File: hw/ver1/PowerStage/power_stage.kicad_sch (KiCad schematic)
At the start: 93 parts, among them J7 Conn_01x02_Socket, Q3 BSS138, Q4 BSS138, Q5 BSS84, Q6 BSS138, U11 74AHC1G126, U12 74AHC1G126, U13 74AHC1G126, U14 74AHC1G126, U15 74AHC1G126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

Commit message: Sync lunch work
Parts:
- U3: footprint Package_QFP:LQFP-64-1EP_10x10mm_P0.5mm_EP6.5x6.5mm -> Package_QFP:LQFP-64-1EP_10x10mm_P0.5mm_EP6.5x6.5mm_ThermalVias
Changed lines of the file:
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@@
 			)
 		)
-		(property "Footprint" "Package_QFP:LQFP-64-1EP_10x10mm_P0.5mm_EP6.5x6.5mm"
+		(property "Footprint" "Package_QFP:LQFP-64-1EP_10x10mm_P0.5mm_EP6.5x6.5mm_ThermalVias"
 			(at 156.21 139.446 0)
 			(effects

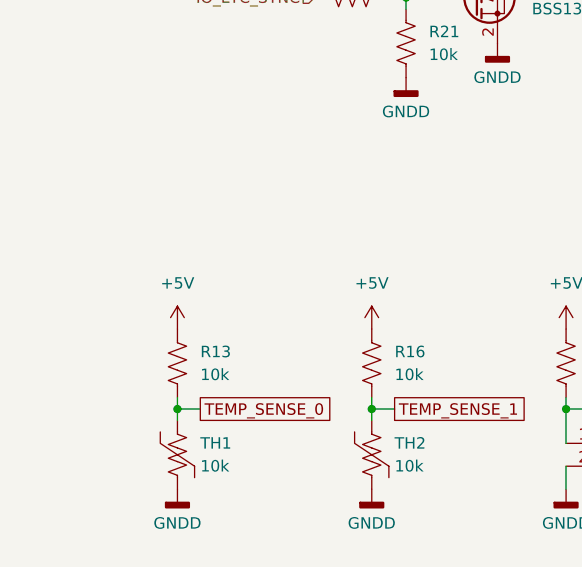
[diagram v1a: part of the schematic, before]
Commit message: Improve low voltage power layout
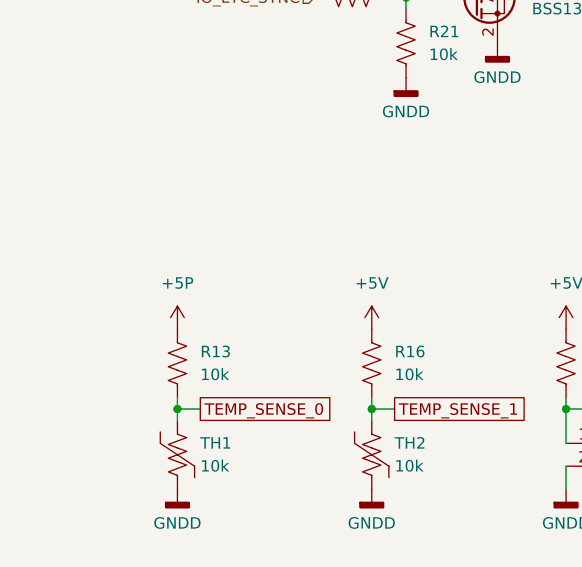
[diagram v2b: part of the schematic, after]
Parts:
- U3: footprint Package_QFP:LQFP-64-1EP_10x10mm_P0.5mm_EP6.5x6.5mm_ThermalVias -> Package_QFP:LQFP-64-1EP_10x10mm_P0.5mm_EP6.5x6.5mm
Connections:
- net +5P: now also R13.2
- net +5V: no longer R13.2
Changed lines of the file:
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@@
+	)
+	(symbol
+		(lib_id "power:+5P")
+		(at 52.07 228.6 0)
+		(unit 1)
+		(exclude_from_sim no)
+		(in_bom yes)
+		(on_board yes)
+		(dnp no)
+		(property "Reference" "#PWR03"
+			(at 52.07 232.41 0)
+			(effects
+				(font
+					(size 1.27 1.27)
+				)
+				(hide yes)
+			)
+		)
+		(property "Value" "+5P"
+			(at 52.07 223.52 0)
+			(effects
+				(font
+					(size 1.27 1.27)
+				)
+			)
+		)
+		(property "Footprint" ""
+			(at 52.07 228.6 0)
+			(effects
+				(font
+					(size 1.27 1.27)
+				)
+				(hide yes)
+			)
+		)
+		(property "Datasheet" ""
+			(at 52.07 228.6 0)
+			(effects
+				(font
+					(size 1.27 1.27)
+				)
+				(hide yes)
+			)
+		)
+		(property "Description" "Power symbol creates a global label with name \"+5P\""
+			(at 52.07 228.6 0)
+			(effects
+				(font
+					(size 1.27 1.27)
+				)
+				(hide yes)
+			)
+		)
+		(pin "1"
+		)
+		(instances
+			(project "IchnaeaV1"
+				(path "/1a8ad36a-4b76-4949-97c2-661f12a0b1d9/2acacade-9567-40f5-9827-bf22bd24fca6"
+					(reference "#PWR03")
+					(unit 1)
+				)
+			)
+		)
 	)
 	(symbol
@@
 			)
 		)
-		(property "Footprint" "Package_QFP:LQFP-64-1EP_10x10mm_P0.5mm_EP6.5x6.5mm_ThermalVias"
+		(property "Footprint" "Package_QFP:LQFP-64-1EP_10x10mm_P0.5mm_EP6.5x6.5mm"
 			(at 156.21 139.446 0)
 			(effects
@@
 					(unit 1)
 				)
-			)
-		)
-	)
-	(symbol
-		(lib_id "power:+5V")
-		(at 52.07 228.6 0)
-		(unit 1)
-		(exclude_from_sim no)
-		(in_bom yes)
-		(on_board yes)
-		(dnp no)
-		(fields_autoplaced yes)
-		(property "Reference" "#PWR03"
-			(at 52.07 232.41 0)
-			(effects
-				(font
-					(size 1.27 1.27)
-				)
-				(hide yes)
-			)
-		)
-		(property "Value" "+5V"
-			(at 52.07 223.52 0)
-			(effects
-				(font
-					(size 1.27 1.27)
-				)
-			)
-		)
-		(property "Footprint" ""
-			(at 52.07 228.6 0)
-			(effects
-				(font
-					(size 1.27 1.27)
-				)
-				(hide yes)
-			)
-		)
-		(property "Datasheet" ""
-			(at 52.07 228.6 0)
-			(effects
-				(font
-					(size 1.27 1.27)
-				)
-				(hide yes)
-			)
-		)
-		(property "Description" "Power symbol creates a global label with name \"+5V\""
-			(at 52.07 228.6 0)
-			(effects
-				(font
-					(size 1.27 1.27)
-				)
-				(hide yes)
-			)
-		)
-		(pin "1"
-		)
-		(instances
-			(project "IchnaeaV1"
-				(path "/1a8ad36a-4b76-4949-97c2-661f12a0b1d9/2acacade-9567-40f5-9827-bf22bd24fca6"
-					(reference "#PWR03")
-					(unit 1)
-				)

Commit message: Sync work
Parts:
- removed J7: Conn_01x02_Socket, Connector_PinSocket_2.54mm:PinSocket_1x02_P2.54mm_Vertical, symbol Connector:Conn_01x02_Socket
- removed R20, R6, R8, R9: 10k, Resistor_SMD:R_0603_1608Metric, symbol Device:R_US
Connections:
- net TEMP_SENSE_2: no longer names the net of U2.12 (A3)
- no-connect marks 4 -> 5

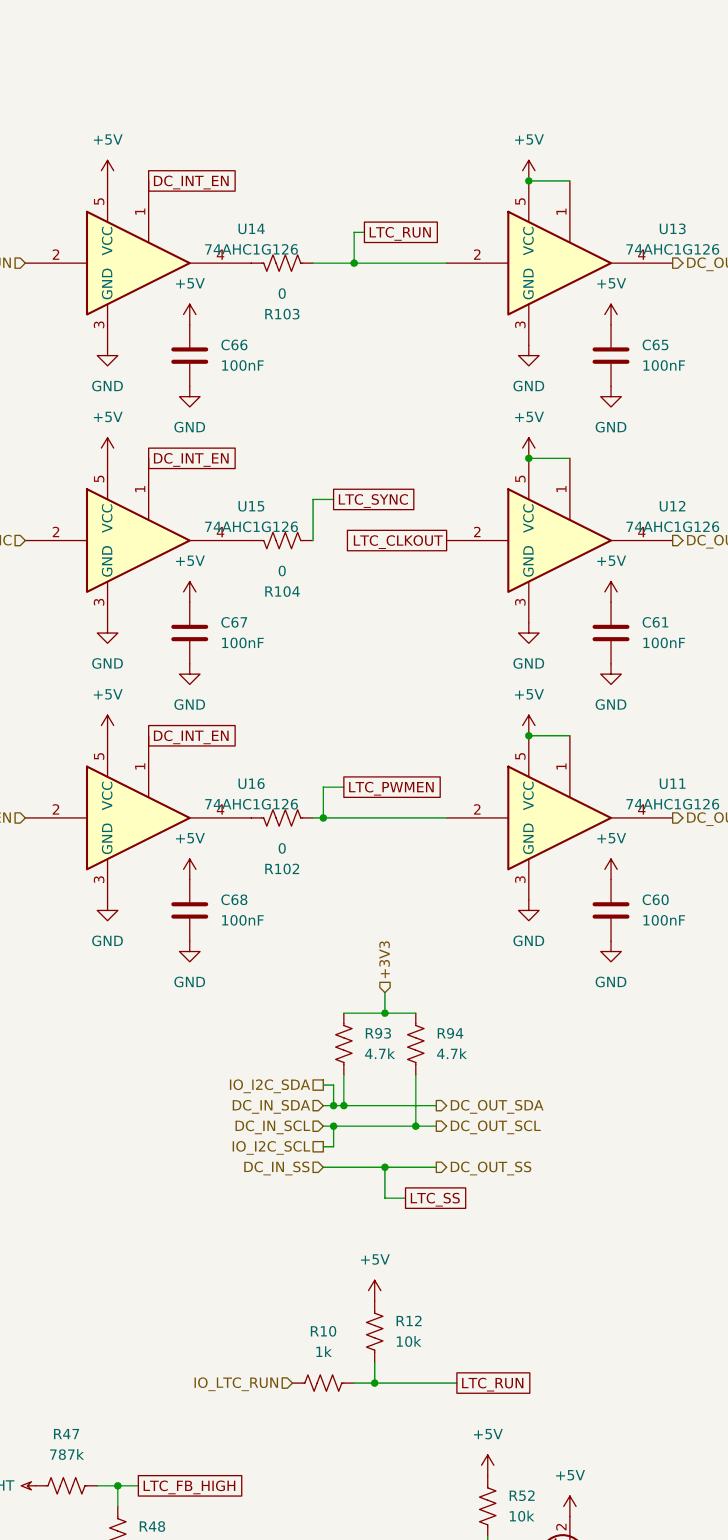
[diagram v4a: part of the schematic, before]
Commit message: Finish the initial route before DRC
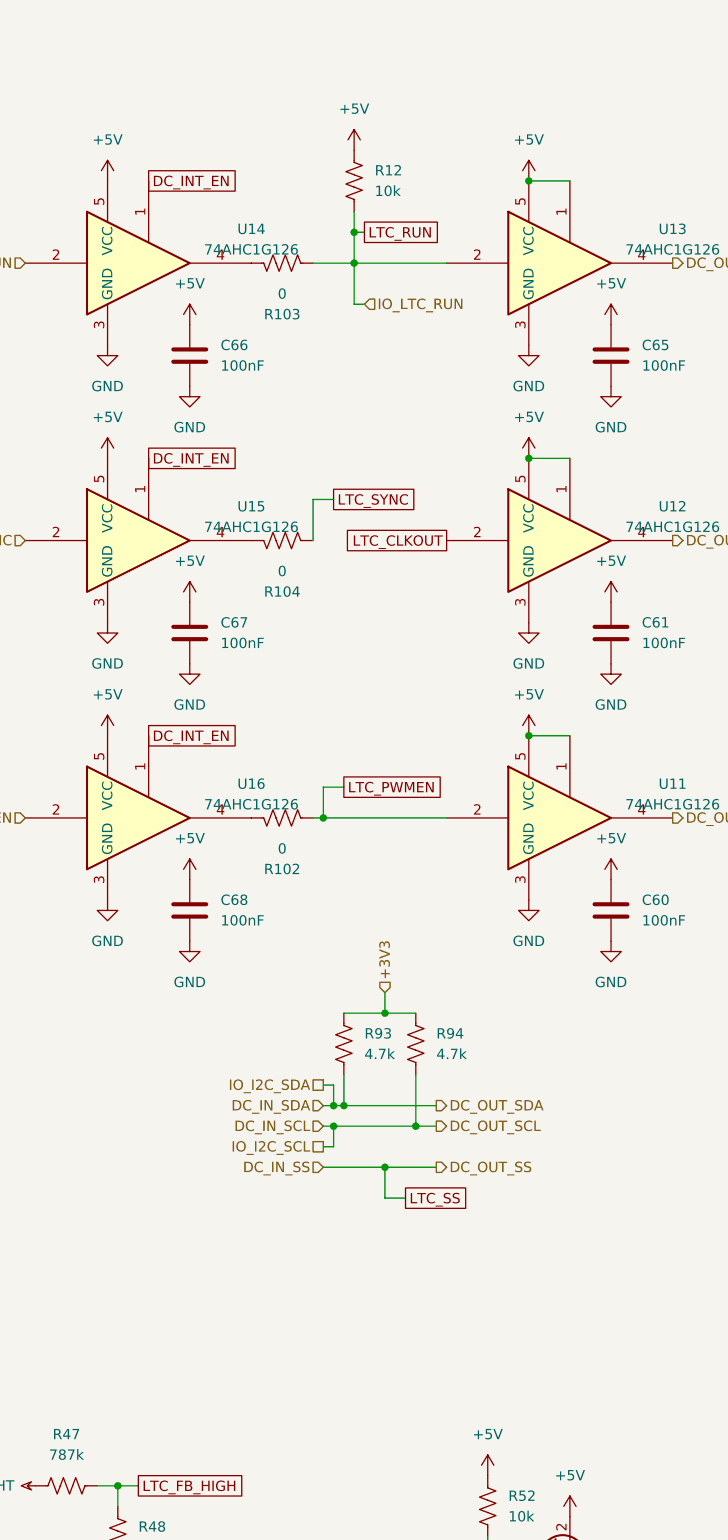
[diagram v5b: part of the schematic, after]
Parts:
- removed R10: 1k, Resistor_SMD:R_0603_1608Metric, symbol Device:R_US
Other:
- moved on the sheet: R12
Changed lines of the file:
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@@
 	)
 	(junction
-		(at 354.33 181.61)
+		(at 373.38 33.02)
 		(diameter 0)
 		(color 0 0 0 0)
 	)
 	(junction
-		(at 373.38 33.02)
+		(at 351.79 39.37)
 		(diameter 0)
 		(color 0 0 0 0)
@@
 	(wire
 		(pts
-			(xy 354.33 179.07) (xy 354.33 181.61)
-		)
-		(stroke
-			(width 0)
-			(type default)
-		)
-	)
-	(wire
-		(pts
 			(xy 215.9 191.77) (xy 215.9 193.04)
 		)
@@
 	(wire
 		(pts
+			(xy 351.79 48.26) (xy 351.79 43.18)
+		)
+		(stroke
+			(width 0)
+			(type default)
+		)
+	)
+	(wire
+		(pts
 			(xy 142.24 233.68) (xy 142.24 229.87)
 		)
@@
 	(wire
 		(pts
-			(xy 354.33 181.61) (xy 364.49 181.61)
-		)
-		(stroke
-			(width 0)
-			(type default)
-		)
-	)
-	(wire
-		(pts
 			(xy 189.23 118.11) (xy 199.39 118.11)
 		)
@@
 	(wire
 		(pts
-			(xy 351.79 181.61) (xy 354.33 181.61)
+			(xy 154.94 133.35) (xy 153.67 133.35)
 		)
 		(stroke
@@
 	(wire
 		(pts
-			(xy 154.94 133.35) (xy 153.67 133.35)
+			(xy 83.82 156.21) (xy 83.82 157.48)
 		)
 		(stroke
@@
 	(wire
 		(pts
-			(xy 83.82 156.21) (xy 83.82 157.48)
+			(xy 351.79 36.83) (xy 351.79 39.37)
 		)
 		(stroke
@@
 	(wire
 		(pts
+			(xy 353.06 48.26) (xy 351.79 48.26)
+		)
+		(stroke
+			(width 0)
+			(type default)
+		)
+	)
+	(wire
+		(pts
 			(xy 260.35 99.06) (xy 260.35 100.33)
 		)
@@
 		)
 	)
-	(global_label "LTC_RUN"
-		(shape passive)
-		(at 364.49 181.61 0)
-		(fields_autoplaced yes)
-		(effects
-			(font
-				(size 1.27 1.27)
-			)
-			(justify left)
-		)
-		(property "Intersheetrefs" "${INTERSHEET_REFS}"
-			(at 374.5282 181.61 0)
-			(effects
-				(font
-					(size 1.27 1.27)
-				)
-				(justify left)
-				(hide yes)
-			)
-		)
-	)
 	(global_label "LTC_ILIM"
 		(shape passive)
@@
 	(hierarchical_label "IO_LTC_RUN"
 		(shape input)
-		(at 344.17 181.61 180)
+		(at 353.06 48.26 0)
 		(fields_autoplaced yes)
 		(effects
@@
 				(size 1.27 1.27)
 			)
-			(justify right)
+			(justify left)
 		)
 	)
@@
 	)
 	(symbol
-		(lib_id "Device:R_US")
-		(at 347.98 181.61 90)
-		(unit 1)
-		(exclude_from_sim no)
-		(in_bom yes)
-		(on_board yes)
-		(dnp no)
-		(fields_autoplaced yes)
-		(property "Reference" "R10"
-			(at 347.98 175.26 90)
-			(effects
-				(font
-					(size 1.27 1.27)
-				)
-			)
-		)
-		(property "Value" "1k"
-			(at 347.98 177.8 90)
-			(effects
-				(font
-					(size 1.27 1.27)
-				)
-			)
-		)
-		(property "Footprint" "Resistor_SMD:R_0603_1608Metric"
-			(at 348.234 180.594 90)
-			(effects
-				(font
-					(size 1.27 1.27)
-				)
-				(hide yes)
-			)
-		)
-		(property "Datasheet" "~"
-			(at 347.98 181.61 0)
-			(effects
-				(font
-					(size 1.27 1.27)
-				)
-				(hide yes)
-			)
-		)
-		(property "Description" "Resistor, US symbol"
-			(at 347.98 181.61 0)
-			(effects
-				(font
-					(size 1.27 1.27)
-				)
-				(hide yes)
-			)
-		)
-		(property "Field-1" ""
-			(at 347.98 181.61 0)
-			(effects
-				(font
-					(size 1.27 1.27)
-				)
-				(hide yes)
-			)
-		)
-		(property "Digikey" "N/A"
-			(at 347.98 181.61 0)
-			(effects
-				(font
-					(size 1.27 1.27)
-				)
-				(hide yes)
-			)
-		)
-		(property "LCSC" "C21190"
-			(at 347.98 181.61 0)
-			(effects
-				(font
-					(size 1.27 1.27)
-				)
-				(hide yes)
-			)
-		)
-		(pin "1"
-		)
-		(pin "2"
-		)
-		(instances
-			(project "IchnaeaV1"
-				(path "/1a8ad36a-4b76-4949-97c2-661f12a0b1d9/2acacade-9567-40f5-9827-bf22bd24fca6"
-					(reference "R10")
-					(unit 1)
-				)
-			)
-		)
-	)
-	(symbol
 		(lib_id "Device:D_Schottky")
 		(at 135.89 20.32 180)
@@
 	(symbol
 		(lib_id "power:+5V")
-		(at 354.33 171.45 0)
+		(at 351.79 29.21 0)
 		(unit 1)
 		(exclude_from_sim no)
@@
 		(fields_autoplaced yes)
 		(property "Reference" "#PWR020"
-			(at 354.33 175.26 0)
+			(at 351.79 33.02 0)
 			(effects
 				(font
@@
 		)
 		(property "Value" "+5V"
-			(at 354.33 166.37 0)
+			(at 351.79 24.13 0)
 			(effects
 				(font
@@
 		)
 		(property "Footprint" ""
-			(at 354.33 171.45 0)
+			(at 351.79 29.21 0)
 			(effects
 				(font
@@
 		)
 		(property "Datasheet" ""
-			(at 354.33 171.45 0)
+			(at 351.79 29.21 0)
 			(effects
 				(font
@@
 		)
 		(property "Description" "Power symbol creates a global label with name \"+5V\""
-			(at 354.33 171.45 0)
+			(at 351.79 29.21 0)
 			(effects
 				(font
@@
 	(symbol
 		(lib_id "Device:R_US")
-		(at 354.33 175.26 180)
+		(at 351.79 33.02 180)
 		(unit 1)
 		(exclude_from_sim no)
@@
 		(fields_autoplaced yes)
 		(property "Reference" "R12"
-			(at 356.87 173.9899 0)
+			(at 354.33 31.7499 0)
 			(effects
 				(font
@@
 		)
 		(property "Value" "10k"
-			(at 356.87 176.5299 0)
+			(at 354.33 34.2899 0)
 			(effects
 				(font
@@
 		)
 		(property "Footprint" "Resistor_SMD:R_0603_1608Metric"
-			(at 353.314 175.006 90)
+			(at 350.774 32.766 90)
 			(effects
 				(font
@@
 		)
 		(property "Datasheet" "~"
-			(at 354.33 175.26 0)
+			(at 351.79 33.02 0)
 			(effects
 				(font
@@
 		)
 		(property "Description" "Resistor, US symbol"
-			(at 354.33 175.26 0)
+			(at 351.79 33.02 0)
 			(effects
 				(font
@@
 		)
 		(property "Field-1" ""
-			(at 354.33 175.26 0)
+			(at 351.79 33.02 0)
 			(effects
 				(font
@@
 		)
 		(property "LCSC" "C25804"
-			(at 354.33 175.26 0)
+			(at 351.79 33.02 0)
 			(effects
 				(font
@@
 		)
 		(property "Digikey" "N/A"
-			(at 354.33 175.26 0)
+			(at 351.79 33.02 0)
 			(effects
 				(font

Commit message: Sync lunch work
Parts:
- C19, C20, C23, C24, C58, C59: value 10uF -> 10uF-100V; LCSC (none) -> N/A
- C64: value 10uF -> 10uF-75V; LCSC (none) -> N/A
- TH1, TH2: value 10k -> 10k-NTC
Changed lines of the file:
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@@
 			)
 		)
-		(property "Value" "10uF"
+		(property "Value" "10uF-100V"
 			(at 245.11 27.9399 0)
 			(effects
@@
 			)
 		)
+		(property "LCSC" "N/A"
+			(at 241.3 26.67 0)
+			(effects
+				(font
+					(size 1.27 1.27)
+				)
+				(hide yes)
+			)
+		)
 		(pin "1"
 		)
@@
 			)
 		)
-		(property "Value" "10uF"
+		(property "Value" "10uF-100V"
 			(at 265.43 27.9399 0)
 			(effects
@@
 			)
 		)
+		(property "LCSC" "N/A"
+			(at 261.62 26.67 0)
+			(effects
+				(font
+					(size 1.27 1.27)
+				)
+				(hide yes)
+			)
+		)
 		(pin "1"
 		)
@@
 			)
 		)
-		(property "Value" "10uF"
+		(property "Value" "10uF-100V"
 			(at 224.79 27.9399 0)
 			(effects
@@
 			)
 		)
+		(property "LCSC" "N/A"
+			(at 220.98 26.67 0)
+			(effects
+				(font
+					(size 1.27 1.27)
+				)
+				(hide yes)
+			)
+		)
 		(pin "1"
 		)
@@
 			)
 		)
-		(property "Value" "10uF"
+		(property "Value" "10uF-100V"
 			(at 234.95 27.9399 0)
 			(effects
@@
 			)
 		)
+		(property "LCSC" "N/A"
+			(at 231.14 26.67 0)
+			(effects
+				(font
+					(size 1.27 1.27)
+				)
+				(hide yes)
+			)
+		)
 		(pin "1"
 		)
@@
 			)
 		)
-		(property "Value" "10k"
+		(property "Value" "10k-NTC"
 			(at 54.61 243.8399 0)
 			(effects
@@
 			)
 		)
-		(property "Value" "10uF"
+		(property "Value" "10uF-75V"
 			(at 144.78 26.6699 0)
 			(effects
@@
 			)
 		)
+		(property "LCSC" "N/A"
+			(at 140.97 25.4 0)
+			(effects
+				(font
+					(size 1.27 1.27)
+				)
+				(hide yes)
+			)
+		)
 		(pin "1"
 		)
@@
 			)
 		)
-		(property "Value" "10uF"
+		(property "Value" "10uF-100V"
 			(at 254 27.9399 0)
 			(effects
@@
 			)
 		)
+		(property "LCSC" "N/A"
+			(at 251.46 26.67 0)
+			(effects
+				(font
+					(size 1.27 1.27)
+				)
+				(hide yes)
+			)
+		)
 		(pin "1"
 		)
@@
 			)
 		)
-		(property "Value" "10uF"
+		(property "Value" "10uF-100V"
 			(at 275.59 27.9399 0)
 			(effects
@@
 			)
 		)
+		(property "LCSC" "N/A"
+			(at 271.78 26.67 0)
+			(effects
+				(font
+					(size 1.27 1.27)
+				)
+				(hide yes)
+			)
+		)
 		(pin "1"
 		)
@@
 			)
 		)
-		(property "Value" "10k"
+		(property "Value" "10k-NTC"
 			(at 76.2 243.8399 0)
 			(effects

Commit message: Add driver support for V1 of the board. Revision HW to v2.0.
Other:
- note added: "V2: Delete"
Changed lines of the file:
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@@
+		)
+	)
+	(text "V2: Delete"
+		(exclude_from_sim no)
+		(at 384.048 107.95 0)
+		(effects
+			(font
+				(size 1.27 1.27)
+			)
 		)
 	)
@@
 		)
 	)
+	(text "V2: Delete"
+		(exclude_from_sim no)
+		(at 384.048 36.83 0)
+		(effects
+			(font
+				(size 1.27 1.27)
+			)
+		)
+	)
 	(text "DRVcc bypass. Place close to pin."
 		(exclude_from_sim no)
 		(at 54.356 38.862 0)
+		(effects
+			(font
+				(size 1.27 1.27)
+			)
+		)
+	)
+	(text "V2: Delete"
+		(exclude_from_sim no)
+		(at 365.76 144.526 0)
+		(effects
+			(font
+				(size 1.27 1.27)
+			)
+		)
+	)
+	(text "V2: Delete"
+		(exclude_from_sim no)
+		(at 280.924 103.886 0)
+		(effects
+			(font
+				(size 1.27 1.27)
+			)
+		)
+	)
+	(text "V2: Delete"
+		(exclude_from_sim no)
+		(at 332.232 106.426 0)
 		(effects
 			(font
@@
 		)
 	)
+	(text "V2: Delete"
+		(exclude_from_sim no)
+		(at 383.286 72.644 0)
+		(effects
+			(font
+				(size 1.27 1.27)
+			)
+		)
+	)
+	(text "V2: Delete"
+		(exclude_from_sim no)
+		(at 332.232 37.846 0)
+		(effects
+			(font
+				(size 1.27 1.27)
+			)
+		)
+	)
+	(text "V2: Delete"
+		(exclude_from_sim no)
+		(at 279.4 139.446 0)
+		(effects
+			(font
+				(size 1.27 1.27)
+			)
+		)
+	)
 	(text "Input Filtering"
 		(exclude_from_sim no)
@@
 		)
 	)
+	(text "V2: Delete"
+		(exclude_from_sim no)
+		(at 332.486 71.374 0)
+		(effects
+			(font
+				(size 1.27 1.27)
+			)
+		)
+	)
